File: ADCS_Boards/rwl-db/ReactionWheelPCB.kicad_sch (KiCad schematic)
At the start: 47 parts, among them J1 PC104_Connector, U1 Conn_1, U10 LM358, U2 Conn_1, U3 Controller 1, U4 Controller 2, U5 Controller 3, U6 Controller 4, U7 Conn_1, U8 Conn_1, U9 LM358

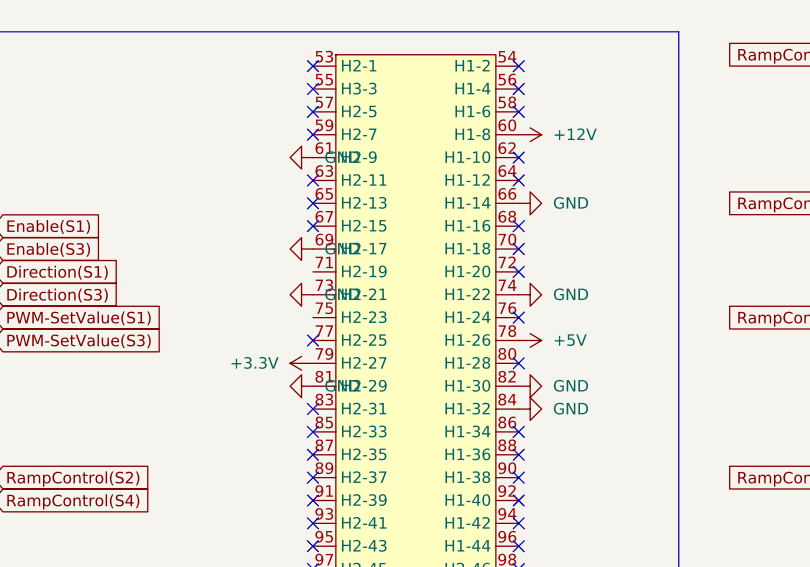
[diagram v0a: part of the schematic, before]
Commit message: adcs: udpated rwl-db and adcs-ctl on behalf of Yasin
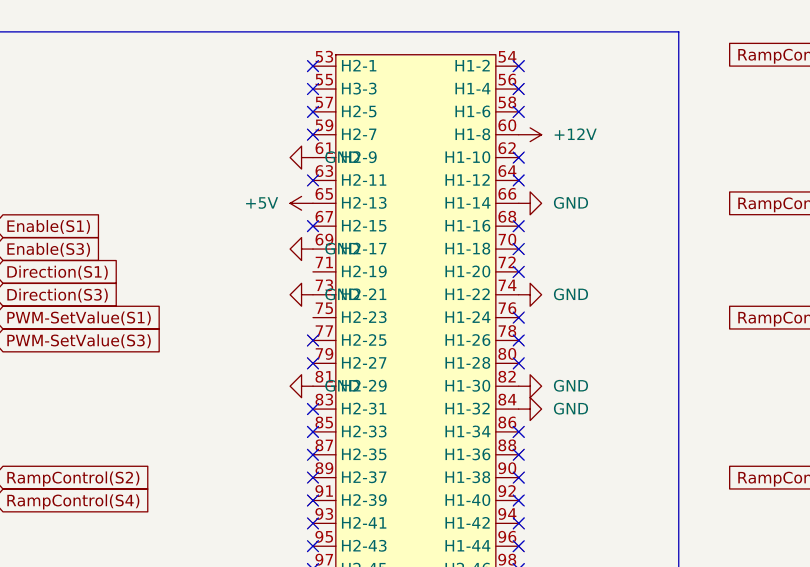
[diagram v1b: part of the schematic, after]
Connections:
- net +5V: now also J1.65 (H2-13); no longer J1.78 (H1-26)
- net +3.3V: no longer names the net of J1.79 (H2-27)
- no-connect marks 99 -> 100
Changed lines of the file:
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@@
   (no_connect (at 66.04 54.61))
   (no_connect (at 74.93 134.62))
+  (no_connect (at 147.32 49.53))
   (no_connect (at 66.04 36.83))
   (no_connect (at 88.9 34.29))
@@
   (no_connect (at 124.46 24.13))
   (no_connect (at 124.46 26.67))
-  (no_connect (at 124.46 34.29))
   (no_connect (at 124.46 36.83))
   (no_connect (at 124.46 49.53))
@@
   (no_connect (at 88.9 54.61))
   (no_connect (at 88.9 31.75))
+  (no_connect (at 124.46 52.07))
   (no_connect (at 113.03 121.92))
   (no_connect (at 88.9 52.07))
@@
     (pin "1")
   )
-  (symbol (lib_id "power:+5V") (at 147.32 49.53 270) (unit 1)
-    (in_bom yes) (on_board yes) (fields_autoplaced)
-    (property "Reference" "#PWR0110" (id 0) (at 143.51 49.53 0)
-      (effects (font (size 1.27 1.27)) hide)
-    )
-    (property "Value" "+5V" (id 1) (at 151.13 49.5299 90)
-      (effects (font (size 1.27 1.27)) (justify left))
-    )
-    (property "Footprint" "" (id 2) (at 147.32 49.53 0)
-      (effects (font (size 1.27 1.27)) hide)
-    )
-    (property "Datasheet" "" (id 3) (at 147.32 49.53 0)
-      (effects (font (size 1.27 1.27)) hide)
-    )
-    (pin "1")
-  )
   (symbol (lib_id "Connector_Generic:Conn_01x11") (at 143.51 172.72 0) (unit 1)
     (in_bom yes) (on_board yes)
@@
     )
     (property "Datasheet" "~" (id 3) (at 17.78 43.18 0)
+      (effects (font (size 1.27 1.27)) hide)
+    )
+    (pin "1")
+  )
+  (symbol (lib_id "power:+5V") (at 124.46 34.29 90) (unit 1)
+    (in_bom yes) (on_board yes)
+    (property "Reference" "#PWR?" (id 0) (at 128.27 34.29 0)
+      (effects (font (size 1.27 1.27)) hide)
+    )
+    (property "Value" "+5V" (id 1) (at 116.84 34.29 90)
+      (effects (font (size 1.27 1.27)) (justify right))
+    )
+    (property "Footprint" "" (id 2) (at 124.46 34.29 0)
+      (effects (font (size 1.27 1.27)) hide)
+    )
+    (property "Datasheet" "" (id 3) (at 124.46 34.29 0)
       (effects (font (size 1.27 1.27)) hide)
     )
@@
     (pin "9")
   )
-  (symbol (lib_id "power:+3.3V") (at 124.46 52.07 90) (unit 1)
-    (in_bom yes) (on_board yes) (fields_autoplaced)
-    (property "Reference" "#PWR0112" (id 0) (at 128.27 52.07 0)
-      (effects (font (size 1.27 1.27)) hide)
-    )
-    (property "Value" "+3.3V" (id 1) (at 120.65 52.0699 90)
-      (effects (font (size 1.27 1.27)) (justify left))
-    )
-    (property "Footprint" "" (id 2) (at 124.46 52.07 0)
-      (effects (font (size 1.27 1.27)) hide)
-    )
-    (property "Datasheet" "" (id 3) (at 124.46 52.07 0)
-      (effects (font (size 1.27 1.27)) hide)
-    )
-    (pin "1")
-  )
   (symbol (lib_id "power:+12V") (at 114.3 101.6 270) (unit 1)
     (in_bom yes) (on_board yes) (fields_autoplaced)
@@
       (reference "#PWR0109") (unit 1) (value "+12V") (footprint "")
     )
-    (path "/3477e712-1d0e-4e65-9506-754086be87a2"
-      (reference "#PWR0110") (unit 1) (value "+5V") (footprint "")
-    )
     (path "/2e114ccf-c96b-4d80-9330-06864bfd2d8a"
       (reference "#PWR0111") (unit 1) (value "+12V") (footprint "")
     )
-    (path "/f129573b-0f3b-40b1-9831-6292558da0a1"
-      (reference "#PWR0112") (unit 1) (value "+3.3V") (footprint "")
-    )
     (path "/8132d6e1-0061-4125-818c-87807617fe30"
       (reference "#PWR0113") (unit 1) (value "GND") (footprint "")
@@
       (reference "#PWR0128") (unit 1) (value "GND") (footprint "")
     )
+    (path "/93d19782-9630-40f0-960b-40eec1b7955c"
+      (reference "#PWR?") (unit 1) (value "+5V") (footprint "")
+    )
     (path "/a114ed39-f7bb-4af6-86cd-c7d161ef8816"

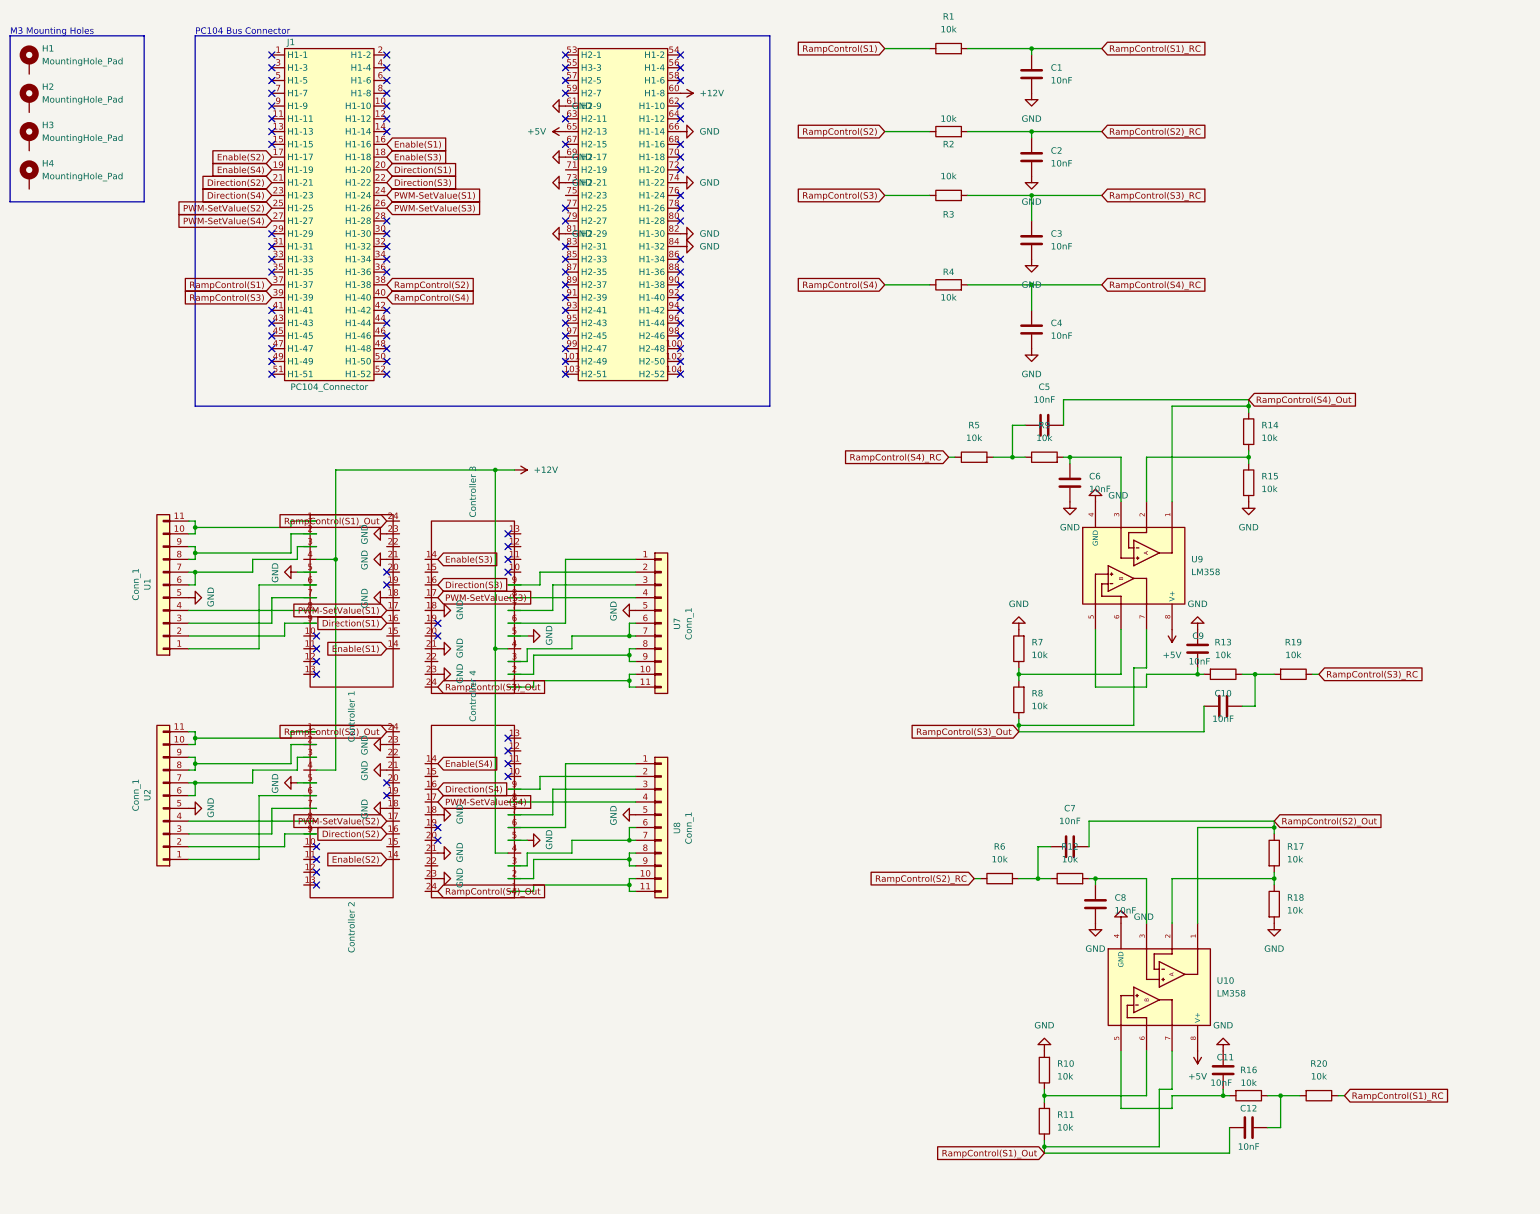
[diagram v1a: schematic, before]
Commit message: adcs: rwl-db: clean up schematic
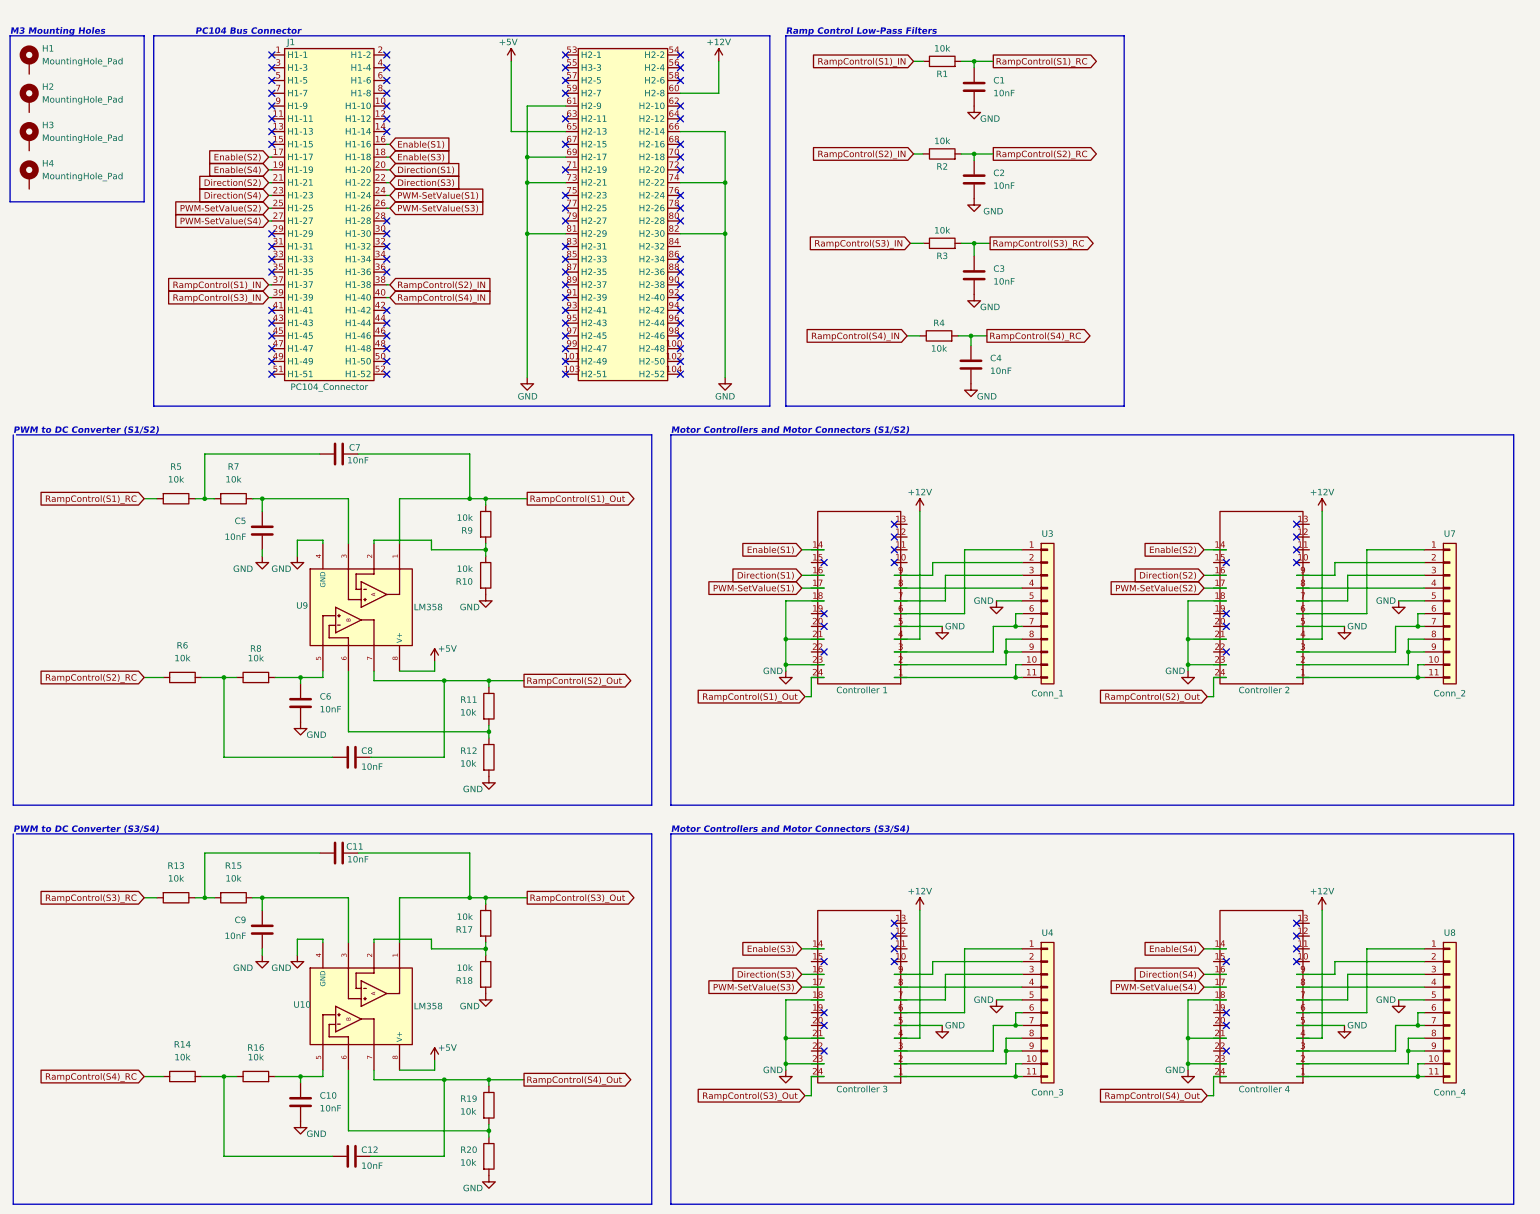
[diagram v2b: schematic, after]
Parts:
- removed U1, U2: Conn_1, Footprints_QSAT:FPC_11_SAT_1-84953-1, symbol Connector_Generic:Conn_01x11
- removed U3: Controller 1, Footprints_QSAT:Escon24.2, symbol UpdatedControllerBoardSchematic-rescue:Escon24.2-symbols-Controller_Board-rescu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
- removed U4: Controller 2, Footprints_QSAT:Escon24.2, symbol UpdatedControllerBoardSchematic-rescue:Escon24.2-symbols-Controller_Board-rescu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
- added U1: Controller 1, Footprints_QSAT:Escon24.2, symbol UpdatedControllerBoardSchematic-rescue:Escon24.2-symbols-Controller_Board-rescu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
- added U2: Controller 3, Footprints_QSAT:Escon24.2, symbol UpdatedControllerBoardSchematic-rescue:Escon24.2-symbols-Controller_Board-rescu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
- added U3: Conn_1, Footprints_QSAT:FPC_11_SAT_1-84953-1, symbol Connector_Generic:Conn_01x11
- added U4: Conn_3, Footprints_QSAT:FPC_11_SAT_1-84953-1, symbol Connector_Generic:Conn_01x11
- J1: footprint pc104-connector:pc104-connector -> qset-footprints:pc104-connector
- U5: value Controller 3 -> Controller 2
- U7: value Conn_1 -> Conn_2
- U8: value Conn_1 -> Conn_4
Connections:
- net +12V: now also U1.4, U2.4
- net Direction(S1): now also U1.16
- net Direction(S2): now also U5.16
- net Direction(S3): now also U2.16; no longer U5.16
- net Enable(S1): now also U1.14
- net Enable(S2): now also U5.14
- net Enable(S3): now also U2.14; no longer U5.14
- net GND: now also C10.2, C5.1, C9.1, R12.2, R20.2, U1.18, U1.21, U1.23, U1.5, U2.18, U2.21, U2.23, U2.5, U3.5 (Pin_5), U4.5 (Pin_5); no longer C11.2, C8.2, C9.2, J1.84 (H1-32), R15.2, R7.2
- net PWM-SetValue(S1): now also U1.17
- net PWM-SetValue(S2): now also U5.17
- net PWM-SetValue(S3): now also U2.17; no longer U5.17
- net RampControl(S1)_Out: now also C7.1, R9.1, U9.1, U1.24; no longer C12.2, R11.1, U10.7
- net RampControl(S1)_RC: now also R5.2; no longer R20.1
- net RampControl(S2)_Out: now also C8.1, R11.1, U5.24, U9.7; no longer C7.2, R17.1, U10.1
- net RampControl(S3)_Out: now also C11.1, R17.1, U10.1, U2.24; no longer C10.2, R8.1, U5.24, U9.7
- net RampControl(S3)_RC: now also R13.2; no longer R19.1
- net RampControl(S4)_Out: now also C12.1, R19.1, U10.7; no longer C5.2, R14.1, U9.1
- net RampControl(S4)_RC: now also R14.1; no longer R5.1
- net at R16.2, U10.5: now also C10.1; no longer C11.1
- net RampControl(S1) renamed RampControl(S1)_IN
- net RampControl(S2) renamed RampControl(S2)_IN
- net RampControl(S3) renamed RampControl(S3)_IN
- net RampControl(S4) renamed RampControl(S4)_IN
- new net: U2.6, U4.1 (Pin_1)
- new net: U2.1, U4.10 (Pin_10), U4.11 (Pin_11)
- new net: U2.9, U4.2 (Pin_2)
- new net: U2.7, U4.3 (Pin_3)
- new net: U2.8, U4.4 (Pin_4)
- new net: U2.3, U4.6 (Pin_6), U4.7 (Pin_7)
- new net: U2.2, U4.8 (Pin_8), U4.9 (Pin_9)
- new net: C6.1, R8.2, U9.5
- new net: R11.2, R12.1, U9.6
- new net: C12.2, R14.2, R16.1
- new net: C8.2, R6.2, R8.1
- new net: C7.2, R5.1, R7.2
- new net: R19.2, R20.1, U10.6
- new net: U1.6, U3.1 (Pin_1)
- new net: U1.1, U3.10 (Pin_10), U3.11 (Pin_11)
- new net: U1.9, U3.2 (Pin_2)
- new net: U1.7, U3.3 (Pin_3)
- new net: U1.8, U3.4 (Pin_4)
- new net: U1.3, U3.6 (Pin_6), U3.7 (Pin_7)
- new net: U1.2, U3.8 (Pin_8), U3.9 (Pin_9)
- new net: C9.2, R15.1, U10.3
- new net: C11.2, R13.1, R15.2
- new net: C5.2, R7.1, U9.3
- new net: R10.1, R9.2, U9.2
- no-connect marks 100 -> 110
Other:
- note added: "Motor Controllers and Motor Connectors (S1/S2)"
- note added: "Motor Controllers and Motor Connectors (S3/S4)"
- note added: "PWM to DC Converter (S1/S2)"
- note added: "PWM to DC Converter (S3/S4)"
- note added: "Ramp Control Low-Pass Filters"
- moved on the sheet: C1, C2, C3, C4, R1, R2, R3, R4
